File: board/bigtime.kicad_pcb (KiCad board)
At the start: 2 copper layers, 90 x 122 mm, 22 parts, among them IC1 NPIC6C596A, IC2 TPS62152, P1 CONN_IN, P2 CONN_OUT, U1 SA40-19, X1 MOUNTING_HOLE, X2 MOUNTING_HOLE, X3 MOUNTING_HOLE, X4 MOUNTING_HOLE

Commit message: test points, footprints, usb
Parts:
- added C10: 100n, agg:0603, F.Cu at (54.8, 131.4)
- added C11: 100n, agg:0603, F.Cu at (85.6, 124.7)
- added C12: 100n, agg:0603, F.Cu at (88.0, 119.1)
- added C13: 100n, agg:0603, F.Cu at (88.0, 114.8)
- added C14: 100n, agg:0603, F.Cu at (79.1, 124.7)
- added C15: 2u2, agg:0603, F.Cu at (81.5, 117.5)
- added C16: 2u2, agg:0603, F.Cu at (48.3, 130.9)
- added C17: 100n, agg:0603, F.Cu at (72.6, 126.6)
- added C18: 100n, agg:0603, F.Cu at (84.5, 110.5)
- added C19: 6p, agg:0603, F.Cu at (67.8, 130.5)
- added C20: 6p, agg:0603, F.Cu at (80.8, 128.6)
- added C21: C, agg:0603, F.Cu at (272.5, 45.0)
- added C22: C, agg:0603, F.Cu at (272.5, 48.5)
- added C23: 22u, agg:1206, F.Cu at (92.1, 78.4)
- added C24: 100n, agg:0603, F.Cu at (84.6, 100.5)
- added C25: 22u, agg:1206, F.Cu at (70.8, 98.4)
- added C26: 100n, agg:0603, F.Cu at (91.9, 90.1)
- added C27: 2u2, agg:0603, F.Cu at (76.5, 103.5)
- added C28: 100n, agg:0603, F.Cu at (108.8, 72.6)
- added C29: 10n 200V, agg:0805, F.Cu at (91.5, 84.0)
- added C30: 10n 200V, agg:0805, F.Cu at (112.6, 66.6)
- added C31: 10n 200V, agg:0805, F.Cu at (78.3, 94.4)
- added C32: 10n 200V, agg:0805, F.Cu at (85.2, 94.4)
- added C33: 100n, agg:0603, F.Cu at (106.9, 79.7)
- added C34: 100n, agg:0603, F.Cu at (98.4, 86.0)
- added C35: C, agg:0603, F.Cu at (78.1, 100.0)
- added C36: 30p, agg:0603, F.Cu at (115.3, 75.7)
- added C37: 30p, agg:0603, F.Cu at (91.1, 100.0)
- added C38: 2u2 60V, agg:1210, F.Cu at (105.1, 66.1)
- added C39: 100n 6.5V, agg:0603, F.Cu at (70.6, 92.5)
- added C40: 100n 60V, agg:0805, F.Cu at (102.1, 73.6)
- added C41: 2u, agg:1206, F.Cu at (77.9, 88.8)
- added C42: 1n, agg:0603, F.Cu at (115.3, 72.2)
- added C43: 2u2, agg:0603, F.Cu at (98.4, 89.9)
- added C44: 15p, agg:0603, F.Cu at (32.4, 44.3)
- added C45: 15p, agg:0603, F.Cu at (42.8, 40.4)
- added C5: 100n, agg:0603, F.Cu at (75.0, 119.6)
- added C6: 1u, agg:0603, F.Cu at (48.3, 133.9)
- added C7: 100n, agg:0603, F.Cu at (80.8, 132.5)
- added C8: 4u7, agg:0603, F.Cu at (81.5, 120.9)
- added C9: 100n, agg:0603, F.Cu at (66.1, 126.6)
- added D10: SS110B, agg:DO-214AA-SMB, F.Cu at (63.4, 85.2)
- added D11: SS110B, agg:DO-214AA-SMB, F.Cu at (63.4, 78.9)
- added D2: 1N4148, agg:SOD-323, F.Cu at (99.9, 80.7)
- added D3: SS110B, agg:DO-214AA-SMB, F.Cu at (85.2, 65.8)
- added D4: SS110B, agg:DO-214AA-SMB, F.Cu at (74.4, 72.1)
- added D5: SS110B, agg:DO-214AA-SMB, F.Cu at (74.4, 65.8)
- added D6: SS110B, agg:DO-214AA-SMB, F.Cu at (62.0, 91.5)
- added D7: SMAJ58A, agg:DO-214AC-SMA, F.Cu at (95.8, 66.2)
- added D8: SS110B, agg:DO-214AA-SMB, F.Cu at (85.2, 72.1)
- added D9: SS110B, agg:DO-214AA-SMB, F.Cu at (74.4, 78.4)
- added IC3: 25AA02E48, agg:SOT-23-6, F.Cu at (67.3, 120.9)
- added IC4: STM32F407VET6, agg:LQFP-100, F.Cu at (54.0, 118.7)
- added IC5: KSZ8081RNx, agg:QFN-24-EP-MICREL, F.Cu at (61.8, 98.7)
- added IC6: MAX5969x, agg:DFN-10-EP-MAX, F.Cu at (94.7, 73.1)
- added IC7: MAX17503, agg:QFN-20-EP-MAX, F.Cu at (84.0, 79.4)
- added J1: RJ45_LEDS, Connect:RJHSE538X, F.Cu at (238.1, 52.0)
- added J2: MICROUSB, agg:MICROUSB_MOLEX_47589-0001, F.Cu at (34.5, 37.8)
- added L2: FB, agg:0603, F.Cu at (48.3, 103.6)
- added L3: 3u3, footprints:ELLATP3R3NB, F.Cu at (63.6, 68.2)
- added L4: 22u, footprints:SRR1260A, F.Cu at (51.6, 69.2)
- added P3: +12V, Connect:BARREL_JACK, F.Cu at (79.2, 37.1)
- added P4: SWD_TC, agg:TC2030-NL, F.Cu at (77.6, 111.9)
- added P5: SWD, agg:FTSH-105-01-F-D-K, F.Cu at (68.4, 112.8)
- added R10: 750, agg:0603, F.Cu at (61.3, 130.9)
- added R11: 33, agg:0603, F.Cu at (113.4, 82.6)
- added R12: 33, agg:0603, F.Cu at (104.9, 93.9)
- added R13: 33, agg:0603, F.Cu at (104.9, 90.4)
- added R14: 33, agg:0603, F.Cu at (111.4, 87.0)
- added R15: 1k, agg:0603, F.Cu at (106.9, 83.5)
- added R16: 1k, agg:0603, F.Cu at (91.9, 93.9)
- added R17: 6k49, agg:0603, F.Cu at (97.6, 97.8)
- added R18: 1k, agg:0603, F.Cu at (91.1, 103.5)
- added R19: 10k, agg:0603, F.Cu at (104.9, 87.0)
- added R20: 75, agg:0603, F.Cu at (98.4, 93.3)
- added R21: 75, agg:0603, F.Cu at (113.4, 79.1)
- added R22: 75, agg:0603, F.Cu at (111.4, 93.9)
- added R23: 75, agg:0603, F.Cu at (97.6, 101.6)
- added R24: 3M3, agg:0603, F.Cu at (110.6, 97.4)
- added R25: 24k9, agg:0603, F.Cu at (104.1, 101.9)
- added R26: 619, agg:0603, F.Cu at (70.0, 101.9)
- added R27: 2M, agg:0603, F.Cu at (111.4, 90.4)
- added R28: 160k, agg:0603, F.Cu at (104.1, 97.7)
- added R29: 10k, agg:0603, F.Cu at (38.9, 44.3)
- added R9: 750, agg:0603, F.Cu at (74.3, 130.4)
- added T1: 749010012A, agg:749010012A, F.Cu at (50.9, 94.0)
- added TP1: +3.3V, agg:SIL-254P-01, F.Cu at (84.0, 33.8)
- added TP2: RESET, agg:SIL-254P-01, F.Cu at (84.0, 40.3)
- added TP3: +48V, agg:SIL-254P-01, F.Cu at (104.0, 33.8)
- added TP4: +12V, agg:SIL-254P-01, F.Cu at (108.6, 33.8)
- added TP5: POE_GOOD, agg:SIL-254P-01, F.Cu at (97.6, 33.8)
- added Y1: 26M, agg:XTAL-20x16, F.Cu at (90.7, 124.4)
- added Y2: 25MHz, agg:XTAL-50x32, F.Cu at (73.8, 84.3)
- added Y3: 32.768k, footprints:XTAL_1206, F.Cu at (43.0, 35.3)
- C1, C2, C3, C4, IC1, IC2, L1: moved to F.Cu
- P1, P2: footprint agg:SIL-254P-06 -> Connect:IDC_Header_Straight_6pins
- R1, R4, R5, R6, R7: value 220R 500mW -> 750; footprint agg:1206 -> agg:0603; moved to F.Cu
- R2: value 220R 500mW -> 380k; footprint agg:1206 -> agg:0603; moved to F.Cu
- R3: value 220R 500mW -> 0; footprint agg:1206 -> agg:0603; moved to F.Cu
- R8: value 400R 500mW -> 750; footprint agg:1206 -> agg:0603; moved to F.Cu
- U1: moved to B.Cu
- X1, X2, X3, X4: value MOUNTING_HOLE -> M3_HOLE
- moved R3 106.8 mm to (178.3, 41.2), turned to 270 degrees
- moved R4 106.8 mm to (168.3, 41.2), turned to 270 degrees
- moved R5 106.8 mm to (163.3, 41.2), turned to 270 degrees
- moved R8 106.8 mm to (183.3, 41.2), turned to 90 degrees
- moved R1 85.3 mm to (178.3, 137.2), turned to 90 degrees
- moved R2 85.3 mm to (183.3, 137.2), turned to 90 degrees
- moved R6 85.3 mm to (168.3, 137.2), turned to 90 degrees
- moved R7 85.3 mm to (163.3, 137.2), turned to 90 degrees
- moved P1 49.4 mm to (136.0, 51.0)
- moved P2 49.0 mm to (209.0, 51.0)
- moved IC2 41.5 mm to (161.3, 73.9)
- moved C3 33.6 mm to (166.0, 77.9)
- moved C4 33.6 mm to (153.5, 77.9)
- moved C2 30.7 mm to (160.4, 79.4)
- moved L1 28.6 mm to (165.5, 80.4)
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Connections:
- C1 pad 1: +3V3 -> GND
- C1 pad 2: GND -> +3V3
- P1 pad 6: +12V -> /V_LED_BUS
- P2 pad 6: +12V -> /V_LED_BUS
- R2 pad 1: Net-(R2-Pad1) -> /V_LED_BUS
- R2 pad 2: Net-(IC1-Pad4) -> Net-(R2-Pad2)
- R3 pad 2: Net-(IC1-Pad5) -> GND
- R4 pad 2: Net-(IC1-Pad6) -> Net-(IC1-Pad4)
- R5 pad 2: Net-(IC1-Pad11) -> Net-(IC1-Pad5)
- R6 pad 2: Net-(IC1-Pad12) -> Net-(IC1-Pad6)
- R7 pad 2: Net-(IC1-Pad13) -> Net-(IC1-Pad11)
- R8 pad 1: Net-(IC1-Pad14) -> Net-(R8-Pad1)
- R8 pad 2: Net-(R8-Pad2) -> Net-(IC1-Pad12)
- U1 pad 1: Net-(R5-Pad1) -> Net-(R7-Pad1)
- U1 pad 10: Net-(R7-Pad1) -> Net-(R9-Pad1)
- U1 pad 2: Net-(R4-Pad1) -> Net-(R6-Pad1)
- U1 pad 3: +12V -> /V_LED_BUS
- U1 pad 4: Net-(R3-Pad1) -> Net-(R5-Pad1)
- U1 pad 5: Net-(R8-Pad2) -> Net-(D1-Pad1)
- U1 pad 6: Net-(R2-Pad1) -> Net-(R4-Pad1)
- U1 pad 8: +12V -> /V_LED_BUS
- U1 pad 9: Net-(R6-Pad1) -> Net-(R8-Pad1)
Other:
- board size 90 x 122 mm -> 90 x 142 mm

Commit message: bump agg-kicad, position mechanical connectors
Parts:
- added D1: 3.9V, agg:SOD-323, F.Cu at (66.6, 160.8)
- added IC8: LDL212DR, agg:SOIC-8, F.Cu at (66.9, 154.3)
- added R30: 33, agg:0603, F.Cu at (74.1, 151.7)
- added R31: 33, agg:0603, F.Cu at (74.1, 155.1)
- added RV1: 100k, footprints:3386P, F.Cu at (57.9, 156.4)
- C21: value C -> 4u7
- C22: value C -> 1u
- R1, R10, R4, R5, R6, R7, R8, R9: value 750 -> 1500
- R2: value 380k -> 866k
- R3: value 0 -> 110k
- moved P5 139.8 mm to (176.5, 24.1), turned to 90 degrees
- moved P4 125.8 mm to (167.8, 24.1), turned to 270 degrees
- moved J2 121.7 mm to (155.0, 21.0), turned to 180 degrees
- moved R3 107.6 mm to (259.6, 111.8)
- moved R4 107.6 mm to (249.6, 111.8)
- moved R5 107.6 mm to (244.6, 111.8)
- moved R8 107.6 mm to (264.6, 111.8)
- moved R1 89.4 mm to (267.7, 138.4)
- moved R2 89.4 mm to (272.7, 138.4)
- moved R6 89.4 mm to (257.7, 138.4)
- moved R7 89.4 mm to (252.7, 138.4)
- moved C1 82.1 mm to (267.7, 94.5)
- moved C2 82.1 mm to (242.2, 86.4)
- moved IC1 82.1 mm to (271.3, 90.3)
- moved C3 82.1 mm to (247.7, 84.9)
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
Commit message: Rough first go at placement minus some shrapnel
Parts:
- added C46: 100n, agg:0603, F.Cu at (173.2, 78.8)
- J1: value RJ45_LEDS -> RJHSE-538B; footprint Connect:RJHSE538X -> footprints:RJHSE538X
- R18: value 1k -> 48k
- moved L4 170.9 mm to (204.8, 98.2)
- moved D6 170.1 mm to (210.0, 43.5), turned to 180 degrees
- moved T1 161.3 mm to (189.2, 44.8), turned to 270 degrees
- moved L3 160.1 mm to (208.5, 65.0), turned to 180 degrees
- moved D10 158.8 mm to (202.6, 48.0), turned to 180 degrees
- moved D11 158.3 mm to (202.5, 43.5), turned to 180 degrees
- moved C31 156.7 mm to (209.2, 38.0)
- moved D4 151.8 mm to (209.8, 52.6), turned to 180 degrees
- moved D5 151.7 mm to (209.8, 48.0), turned to 180 degrees
- moved C39 150.7 mm to (206.0, 87.2), turned to 180 degrees
- moved R26 150.6 mm to (202.0, 70.0), turned to 90 degrees
- moved R29 149.6 mm to (172.2, 26.8), turned to 90 degrees
- moved C32 149.5 mm to (209.2, 40.0)
- moved D9 145.6 mm to (202.5, 52.6), turned to 180 degrees
- moved R23 144.2 mm to (212.8, 40.0)
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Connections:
- C38 pad 2: /ethernet/+48V -> +48V
- IC4 pad 16: Net-(IC4-Pad16) -> /RMII_MDC
- IC4 pad 24: Net-(IC4-Pad24) -> /RMII_REF_CLK
- IC4 pad 25: Net-(IC4-Pad25) -> /RMII_MDIO
- IC4 pad 32: Net-(IC4-Pad32) -> /RMII_CRS_DV
- IC4 pad 33: Net-(IC4-Pad33) -> /RMII_RXD0
- IC4 pad 34: Net-(IC4-Pad34) -> /RMII_RXD1
- IC4 pad 48: Net-(IC4-Pad48) -> /RMII_TXEN
- IC4 pad 68: Net-(IC4-Pad68) -> /USB_VBUS
- IC4 pad 70: Net-(IC4-Pad70) -> /USB_D-
- IC4 pad 71: Net-(IC4-Pad71) -> /USB_D+
- IC4 pad 77: Net-(IC4-Pad77) -> /ROM_CS
- IC4 pad 78: Net-(IC4-Pad78) -> /ROM_SCK
- IC4 pad 79: Net-(IC4-Pad79) -> /ROM_MISO
- IC4 pad 80: Net-(IC4-Pad80) -> /ROM_MOSI
- IC7 pad 1: /ethernet/+48V -> +48V
- IC7 pad 2: /ethernet/+48V -> +48V
- IC7 pad 3: /ethernet/+48V -> +48V
- J1 pad 10: Net-(J1-Pad10) -> /ethernet/LINK_LED
- J1 pad 11: /TRAFFIC_LED -> GND
- J1 pad 9: /ethernet/LINK_LED -> Net-(J1-Pad9)
- L3 pad 1: /ethernet/+48V -> +48V
- R15 pad 2: Net-(J1-Pad10) -> Net-(J1-Pad9)
- R18 pad 2: +3V3 -> +48V
- R24 pad 1: /ethernet/+48V -> +48V
- R30 pad 1: Net-(R30-Pad1) -> /RMII_TXD1
- R30 pad 2: /RMII_TXD1 -> Net-(IC4-Pad52)
- R31 pad 1: Net-(R31-Pad1) -> /RMII_TXD0
- R31 pad 2: /RMII_TXD0 -> Net-(IC4-Pad51)
- TP3 pad 1: /ethernet/+48V -> +48V
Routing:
- net GND: track 0.00 -> 79.0 mm, vias 0 -> 15
- net /RMII_TXD0: track 0.00 -> 64.8 mm
- net /RMII_TXD1: track 0.00 -> 56.3 mm
- net Net-(C40-Pad1): track 0.00 -> 45.5 mm
- net /ethernet/VA2: track 0.00 -> 42.1 mm
- net +12V: track 0.00 -> 41.7 mm
- net /ethernet/VA1: track 0.00 -> 41.4 mm, vias 0 -> 2
- net Net-(C40-Pad2): track 0.00 -> 39.8 mm
- net /USB_D-: track 0.00 -> 33.6 mm
- net /USB_D+: track 0.00 -> 33.5 mm
- net /ethernet/VB2: track 0.00 -> 33.5 mm, vias 0 -> 2
- net /ethernet/VB1: track 0.00 -> 31.6 mm, vias 0 -> 2
- net /SWDCLK: track 0.00 -> 31.3 mm, vias 0 -> 1
- net Net-(IC5-Pad3): track 0.00 -> 26.0 mm
- net /SWDIO: track 0.00 -> 25.3 mm
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- added copper zone on B.Cu, net GND

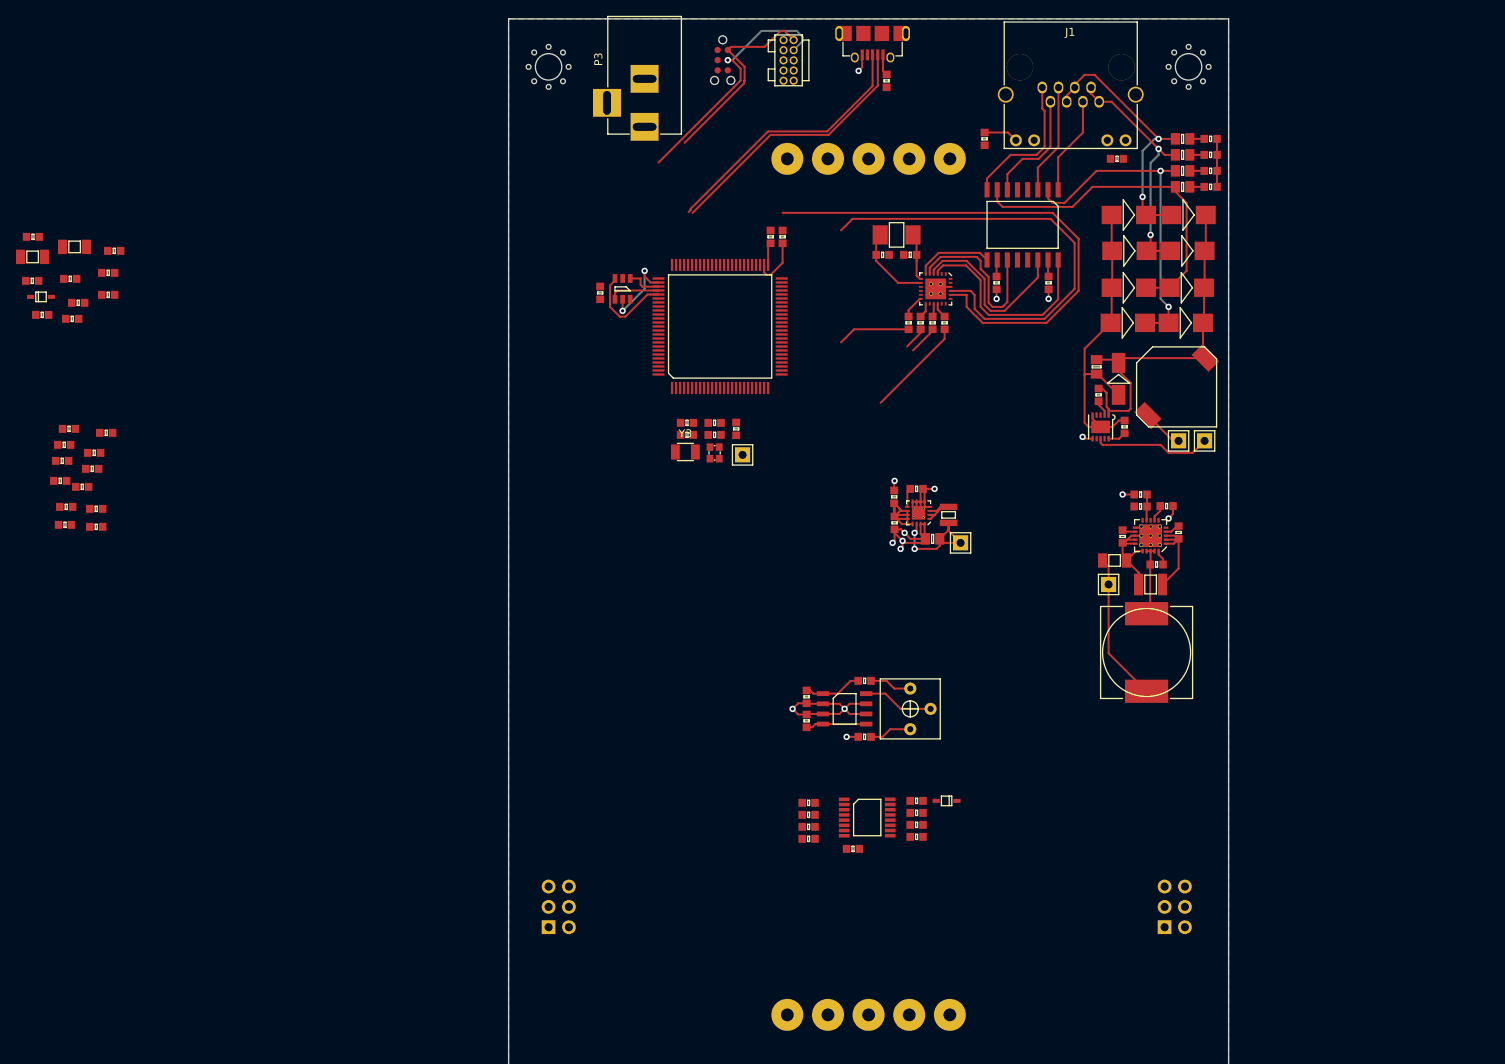
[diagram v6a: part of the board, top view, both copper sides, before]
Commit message: nearly done first route
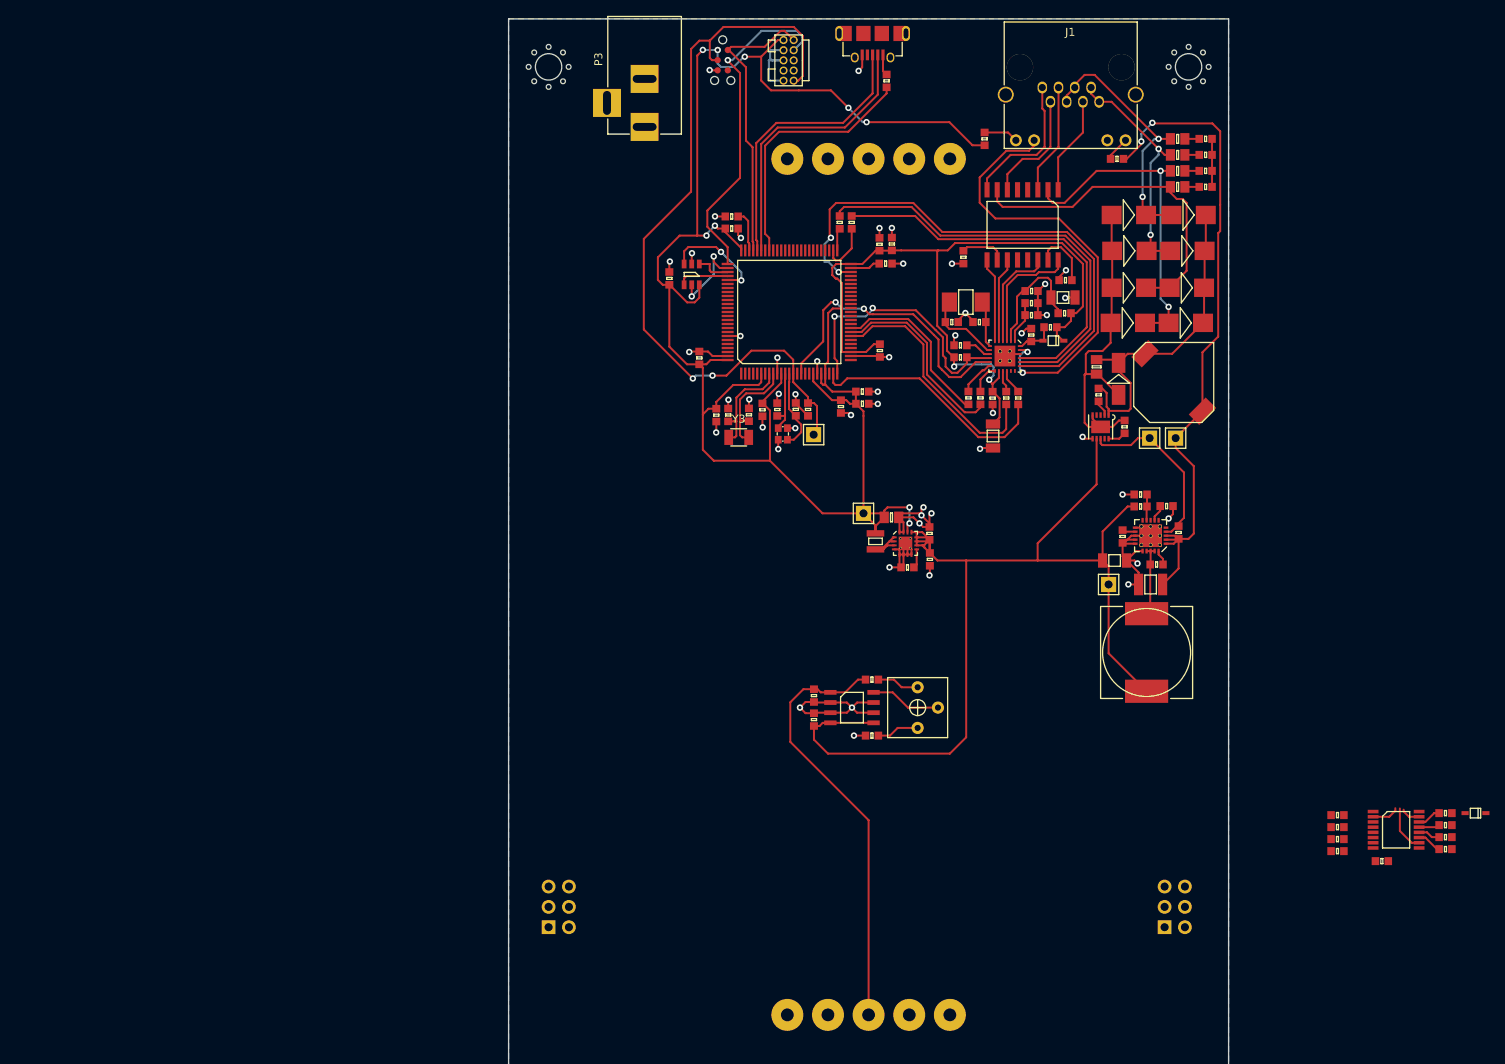
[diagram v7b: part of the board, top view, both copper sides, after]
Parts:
- moved L2 129.3 mm to (194.5, 55.8)
- moved C23 128.9 mm to (194.3, 53.8)
- moved D2 126.7 mm to (193.1, 59.2), turned to 180 degrees
- moved R19 126.0 mm to (192.7, 57.5), turned to 180 degrees
- moved C24 124.9 mm to (190.4, 53.0)
- moved C35 119.9 mm to (190.3, 58.5), turned to 90 degrees
- moved C25 117.2 mm to (185.6, 71.1), turned to 270 degrees
- moved C26 116.3 mm to (185.5, 66.4), turned to 270 degrees
- moved C28 115.5 mm to (190.4, 56.0)
- moved C27 114.8 mm to (190.4, 54.5)
- moved R16 110.5 mm to (181.5, 61.3)
- moved R17 106.7 mm to (181.5, 59.8), turned to 180 degrees
- moved C15 105.2 mm to (172.1, 49.6)
- moved C10 104.2 mm to (171.4, 47.2), turned to 90 degrees
- moved C13 104.2 mm to (171.4, 60.5), turned to 270 degrees
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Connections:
- IC4 pad 89: Net-(IC4-Pad89) -> /SHCP
- IC4 pad 90: Net-(IC4-Pad90) -> /STCP
- IC4 pad 91: Net-(IC4-Pad91) -> /DS_IN
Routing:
- net +3V3: track 15.8 -> 318.3 mm, vias 2 -> 11
- net /~RST: track 0.00 -> 97.1 mm, vias 0 -> 2
- net +12V: track 41.7 -> 135.2 mm
- net GND: track 79.0 -> 149.5 mm, vias 15 -> 49
- net /RMII_TXEN: track 0.00 -> 67.2 mm, vias 0 -> 2
- net +48V: track 16.9 -> 82.6 mm, vias 0 -> 2
- net /ethernet/LINK_LED: track 0.00 -> 55.6 mm, vias 0 -> 2
- net /V_LED_BUS: track 7.27 -> 54.0 mm
- net /RMII_MDC: track 0.00 -> 36.9 mm, vias 0 -> 2
- net /RMII_MDIO: track 0.00 -> 34.3 mm, vias 0 -> 2
- net /USB_VBUS: track 0.00 -> 32.0 mm
- net /RMII_CRS_DV: track 3.66 -> 31.1 mm
- net /RMII_RXD0: track 2.85 -> 24.3 mm
- net /RMII_REF_CLK: track 12.5 -> 30.9 mm
- net Net-(C23-Pad1): track 0.00 -> 15.9 mm
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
